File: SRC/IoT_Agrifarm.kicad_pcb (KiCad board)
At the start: 4 copper layers, 53.3 x 57.2 mm, 118 parts, among them J101 J_PUMP, J102 J_PANEL, J103 Conn_NPK, J104 USB_C_Receptacle_USB2.0, J401 Conn_PH, J402 Conn_MOISTURE, Q101 AO3401A, Q102 IRLZ44N, Q201 AO3401A, Q401 Q_Photo_NPN, SW301 SW_Push, SW302 SW_BOOT, U101 AP2171W, U102 USBLC6-2P6, U201 DW01A, U202 8205A, U203 BQ25672RQMR, U204 DW01A, U205 8205A, U206 L78L05, U207 SD8942, U301 RP2040, U302 25Q128, U401 DS18B20, U402 DHT11, U403 MAX3362, U501 Ai-Thinker-Ra-02, Y301 12MHz

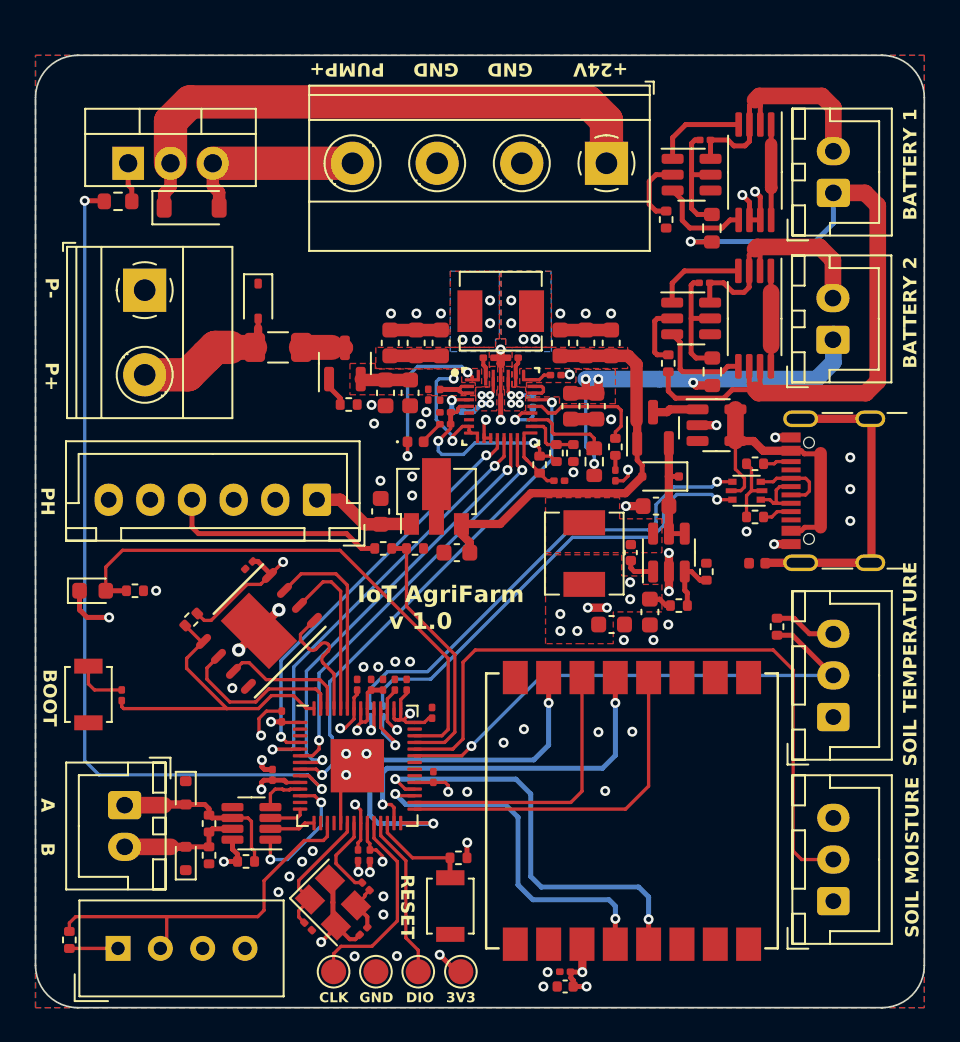
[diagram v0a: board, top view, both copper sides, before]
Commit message: Version 2 - Added 24V 2A Boost converter for water pump
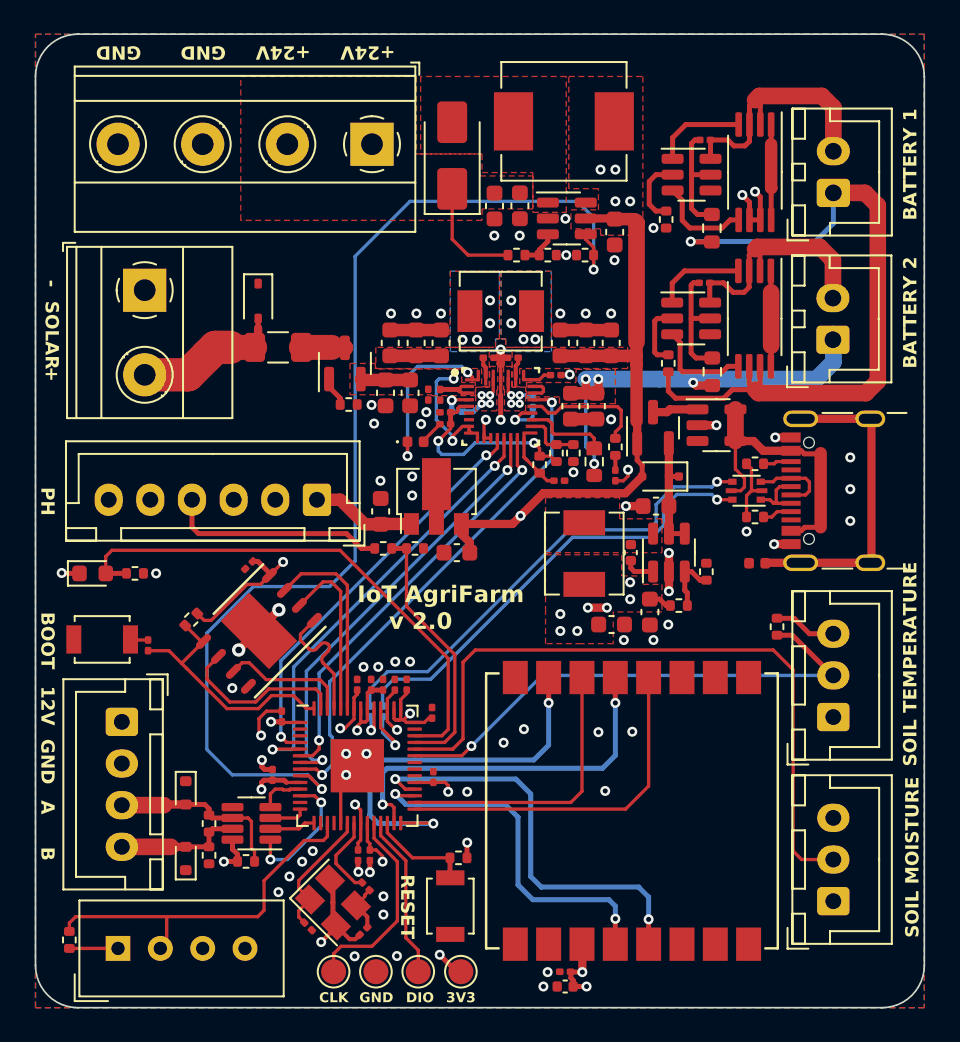
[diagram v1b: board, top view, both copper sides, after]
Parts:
- removed the D101 at (126.2, 58.7)
- removed Q102: IRLZ44N, Package_TO_SOT_THT:TO-220-3_Vertical
- removed the R101 at (121.8, 58.3)
- added C601: 10u, Capacitor_SMD:C_0603_1608Metric, F.Cu at (151.6, 60.1)
- added C602: 10u, Capacitor_SMD:C_0603_1608Metric, F.Cu at (145.9, 58.6)
- added C603: 10u, Capacitor_SMD:C_0603_1608Metric, F.Cu at (144.4, 58.6)
- added D601: SS34, Diode_SMD:D_SMA, F.Cu at (141.8, 55.5)
- added L601: 10u, Inductor_SMD:L_Sunlord_MWSA0603S, F.Cu at (148.6, 53.5)
- added R601: 200K, Resistor_SMD:R_0402_1005Metric, F.Cu at (145.7, 61.5)
- added R602: 1M, Resistor_SMD:R_0402_1005Metric, F.Cu at (149.8, 61.5)
- added R603: 5K1, Resistor_SMD:R_0402_1005Metric, F.Cu at (147.6, 61.5)
- added U601: SY7208, Package_TO_SOT_SMD:SOT-23-6, F.Cu at (148.7, 59.3)
- J103: footprint Connector_JST:JST_XH_B2B-XH-A_1x02_P2.50mm_Vertical -> Connector_JST:JST_XH_B4B-XH-A_1x04_P2.50mm_Vertical
- R213: renamed from R212; value R_Small -> 100K
- R214: renamed from R213; value R_Small -> 25K5
- moved J101 14.1 mm to (137.0, 54.9)
- moved J103 5.00 mm to (122.0, 89.5)
- moved SW302 3.40 mm to (120.8, 84.6), turned to 0 degrees
- moved R306 3.39 mm to (123.6, 84.9)
- moved Q401 1.04 mm to (120.3, 80.6)
- moved R403 1.04 mm to (122.8, 80.6)
- renumbered D102 to D101, R102 to R101, R103 to R102, R104 to R103, R215 to R211, R211 to R212
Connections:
- C214 pad 1: /IOT_AGRIFARM_POWER/VSYS -> +12V
- C215 pad 1: /IOT_AGRIFARM_POWER/VSYS -> +12V
- C216 pad 1: /IOT_AGRIFARM_POWER/VSYS -> +12V
- C217 pad 1: /IOT_AGRIFARM_POWER/VSYS -> +12V
- C221 pad 1: /IOT_AGRIFARM_POWER/VSYS -> +12V
- D202 pad 2: /IOT_AGRIFARM_POWER/VSYS -> +12V
- J101 pad 1: /+24V -> /REGULATOR_SWITCHING_SY7208/VOUT_24V
- J101 pad 2: GND -> /REGULATOR_SWITCHING_SY7208/VOUT_24V
- J101 pad 4: /PUMP+ -> GND
- J103 pad 1: /IOT_AGRIFARM_SENSORS/NPK_A -> +12V
- J103 pad 2: /IOT_AGRIFARM_SENSORS/NPK_B -> GND
- Q201 pad 1: /IOT_AGRIFARM_POWER/VSYS -> +12V
- U203 pad 25: /IOT_AGRIFARM_POWER/VSYS -> +12V
- U206 pad 3: /IOT_AGRIFARM_POWER/VSYS -> +12V
- U301 pad 9: /PUMP_EN -> /MCU_RP2040/GPIO7
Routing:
- net +12V: track 0.00 -> 73.1 mm, vias 0 -> 5
- net /MCU_RP2040/GPIO7: track 0.00 -> 67.0 mm, vias 0 -> 2
- net /PUMP_EN: track 51.4 -> 0.00 mm, vias 2 -> 0
- net /+24V: track 35.0 -> 0.00 mm
- net /IOT_AGRIFARM_POWER/VSYS: track 26.9 -> 0.00 mm
- net /PUMP+: track 11.2 -> 0.00 mm
- net /REGULATOR_SWITCHING_SY7208/VOUT_24V: track 0.00 -> 6.77 mm
- net /MCU_RP2040/QSPI_SS: track 19.4 -> 15.3 mm
- net Net-(Q102-G): track 2.38 -> 0.00 mm
- net Net-(U601-FB): track 0.00 -> 2.32 mm
- net Net-(R306-Pad2): track 3.22 -> 1.07 mm
- net +3V3: track 49.7 -> 47.7 mm
- net /IOT_AGRIFARM_SENSORS/LIGHT_SENSOR: track 32.7 -> 32.1 mm
- net GND: vias 67 -> 73
- added copper zone on F.Cu, net +12V
- added copper zone on In1.Cu, net +12V
- added copper zone on F.Cu, net /REGULATOR_SWITCHING_SY7208/SW_24V
- added copper zone on F.Cu, net /REGULATOR_SWITCHING_SY7208/VOUT_24V
- removed copper zone on F.Cu, net /IOT_AGRIFARM_POWER/VSYS
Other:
- board size 53.3 x 57.2 mm -> 53.3 x 58.4 mm
- board text added: "+"
- board text added: "-"
- board text added: "12V"
- board text added: "IoT AgriFarm v 2.0"
- board text added: "SOLAR"
- board text removed: "IoT AgriFarm v 1.0"
- board text removed: "P+"
- board text removed: "P-"
- board text removed: "PUMP+"
